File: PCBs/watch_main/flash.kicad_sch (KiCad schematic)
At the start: 1 part, among them IC1001 S26HS512TGABHI000

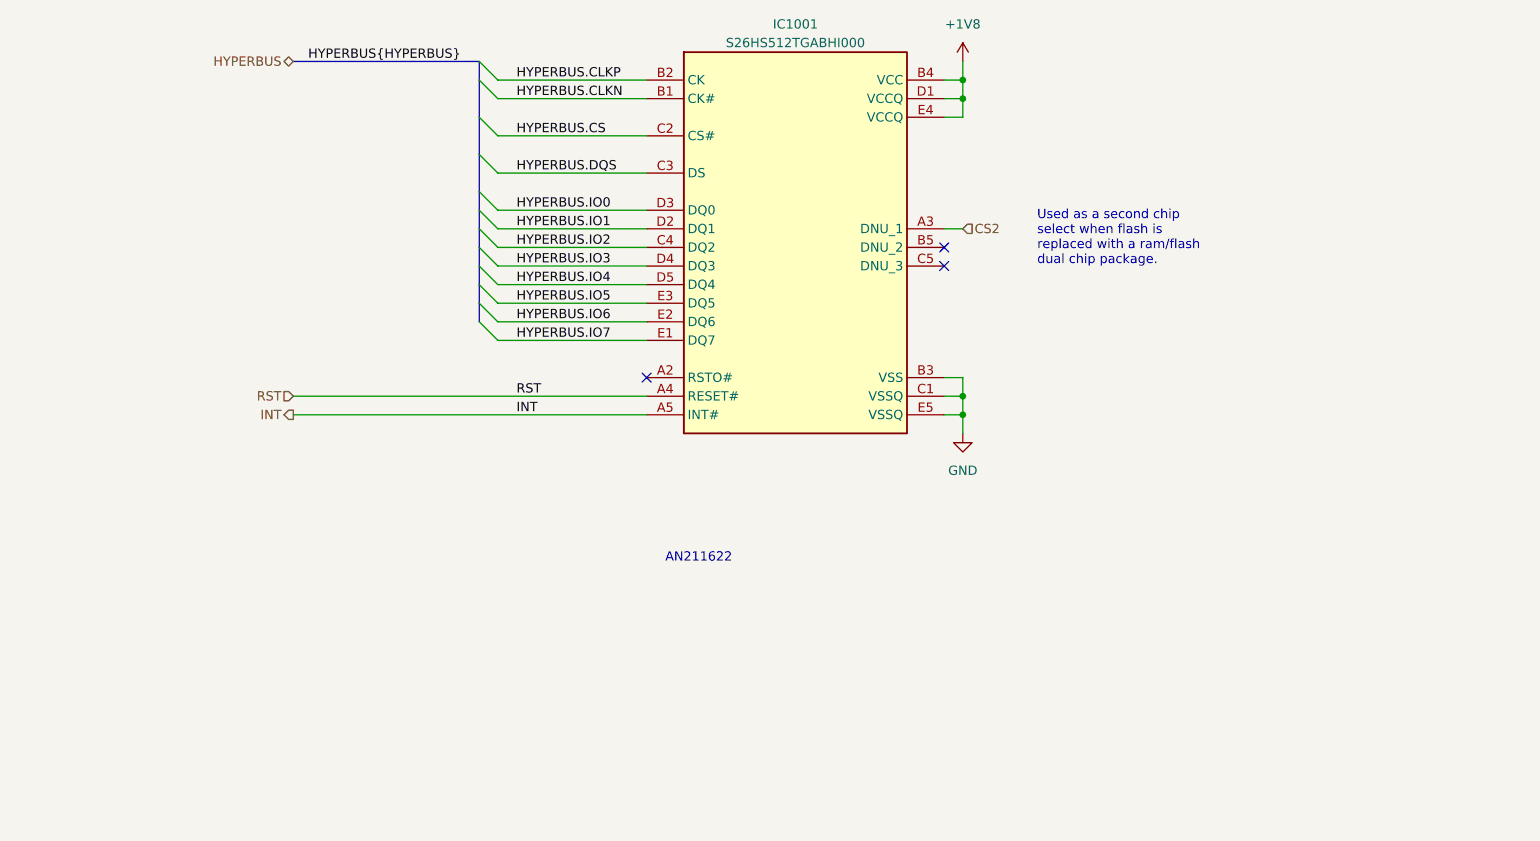
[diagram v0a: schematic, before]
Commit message: Created firmware project
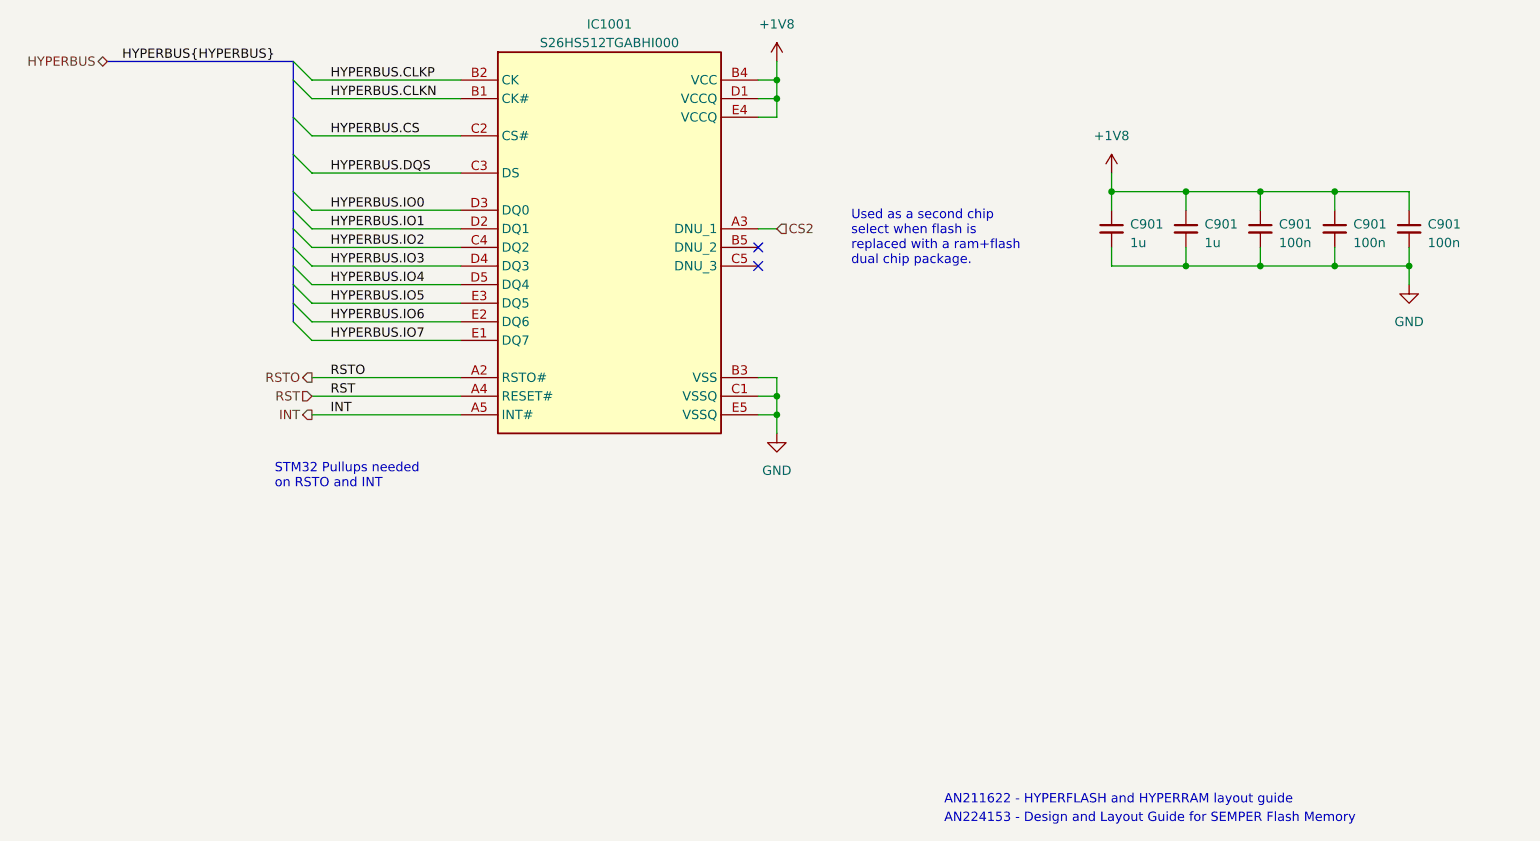
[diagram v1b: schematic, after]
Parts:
- added C901 (x2): 1u, Capacitor_SMD:C_0402_1005Metric, symbol Device:C_Small
- added C901 (x3): 100n, Capacitor_SMD:C_0402_1005Metric, symbol Device:C_Small
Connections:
- net +1V8: now also C901.1, C901.1, C901.1, C901.1, C901.1
- net GND: now also C901.2, C901.2, C901.2, C901.2, C901.2
- net RSTO: now reaches IC1001.A2 (RSTO#)
- no-connect marks 3 -> 2
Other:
- note added: "AN211622 - HYPERFLASH and HYPERRAM layout guide"
- note added: "AN224153 - Design and Layout Guide for SEMPER Flash Memory"
- note added: "STM32 Pullups needed on RSTO and INT"
- note added: "Used as a second chip select when flash is replaced with a ram+flash dual chip package."
- note removed: "AN211622"
- note removed: "Used as a second chip select when flash is replaced with a ram/flash dual chip package."
- moved on the sheet: IC1001

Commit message: Progress with schematic and RFID simulations
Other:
- moved on the sheet: C901

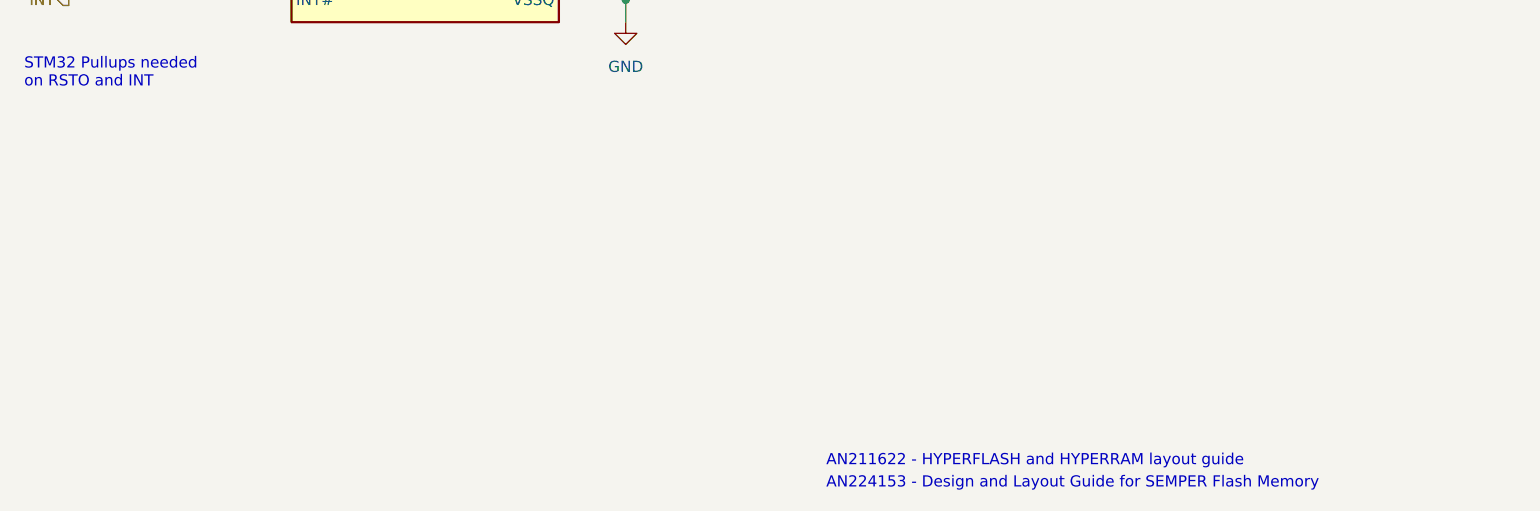
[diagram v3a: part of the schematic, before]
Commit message: Schematic finished and BOM started
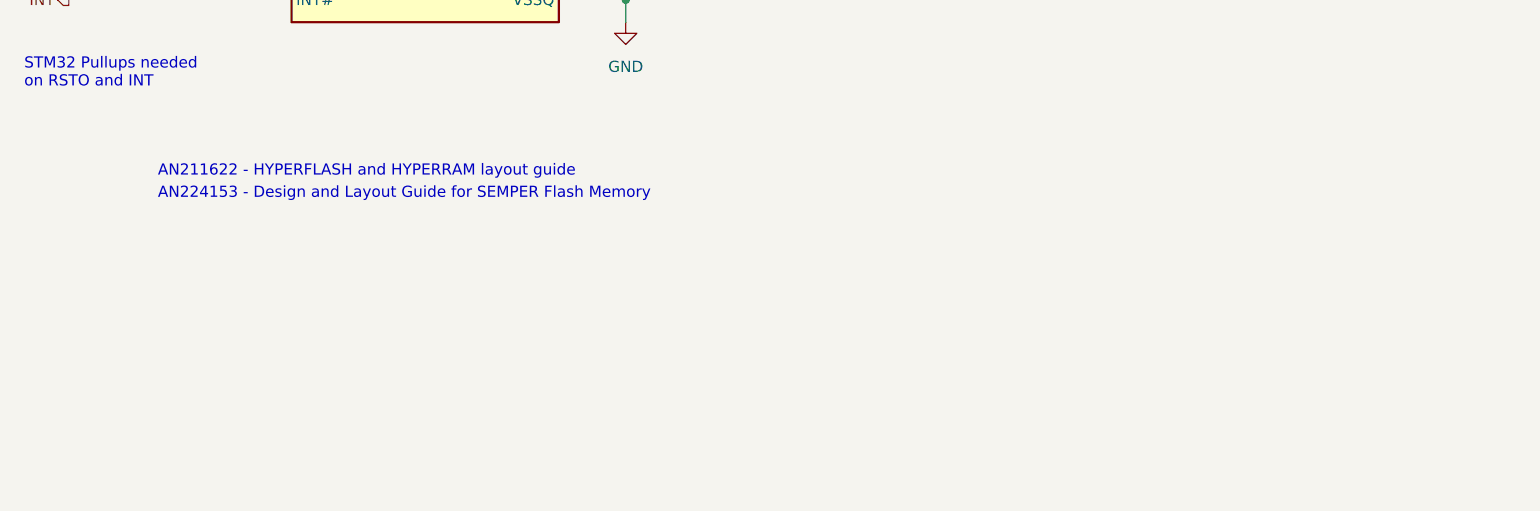
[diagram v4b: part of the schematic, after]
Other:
- title: (none) -> Watch Flash
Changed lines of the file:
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@@
 (kicad_sch (version 20230121) (generator eeschema)
   (paper "A4")
+  (title_block
+    (title "Watch Flash")
+    (date "2023-12-21")
+    (rev "1")
+    (comment 1 "Checked by Ben Smith on 21/12/23")
+  )
   (junction (at 154.94 114.3) (diameter 0) (color 0 0 0 0)
   )
@@
   )
   (text "AN224153 - Design and Layout Guide for SEMPER Flash Memory"
-    (at 177.8 172.72 0)
+    (at 101.6 139.7 0)
     (effects (font (size 1.27 1.27)) (justify left bottom))
   )
@@
     (effects (font (size 1.27 1.27)) (justify left bottom))
   )
-  (text "AN211622 - HYPERFLASH and HYPERRAM layout guide" (at 177.8 170.18 0)
-    (effects (font (size 1.27 1.27)) (justify left bottom))
-  )
+  (text "AN211622 - HYPERFLASH and HYPERRAM layout guide" (at 101.6 137.16 0)
+    (effects (font (size 1.27 1.27)) (justify left bottom))
+  )
